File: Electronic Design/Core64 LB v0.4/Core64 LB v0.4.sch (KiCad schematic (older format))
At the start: 12 parts, among them J4 TSM-106-03-T-DV‎, U2 Teensy3.2, U3 M24C01-RMN, U4 SN74LV1T125DBVR

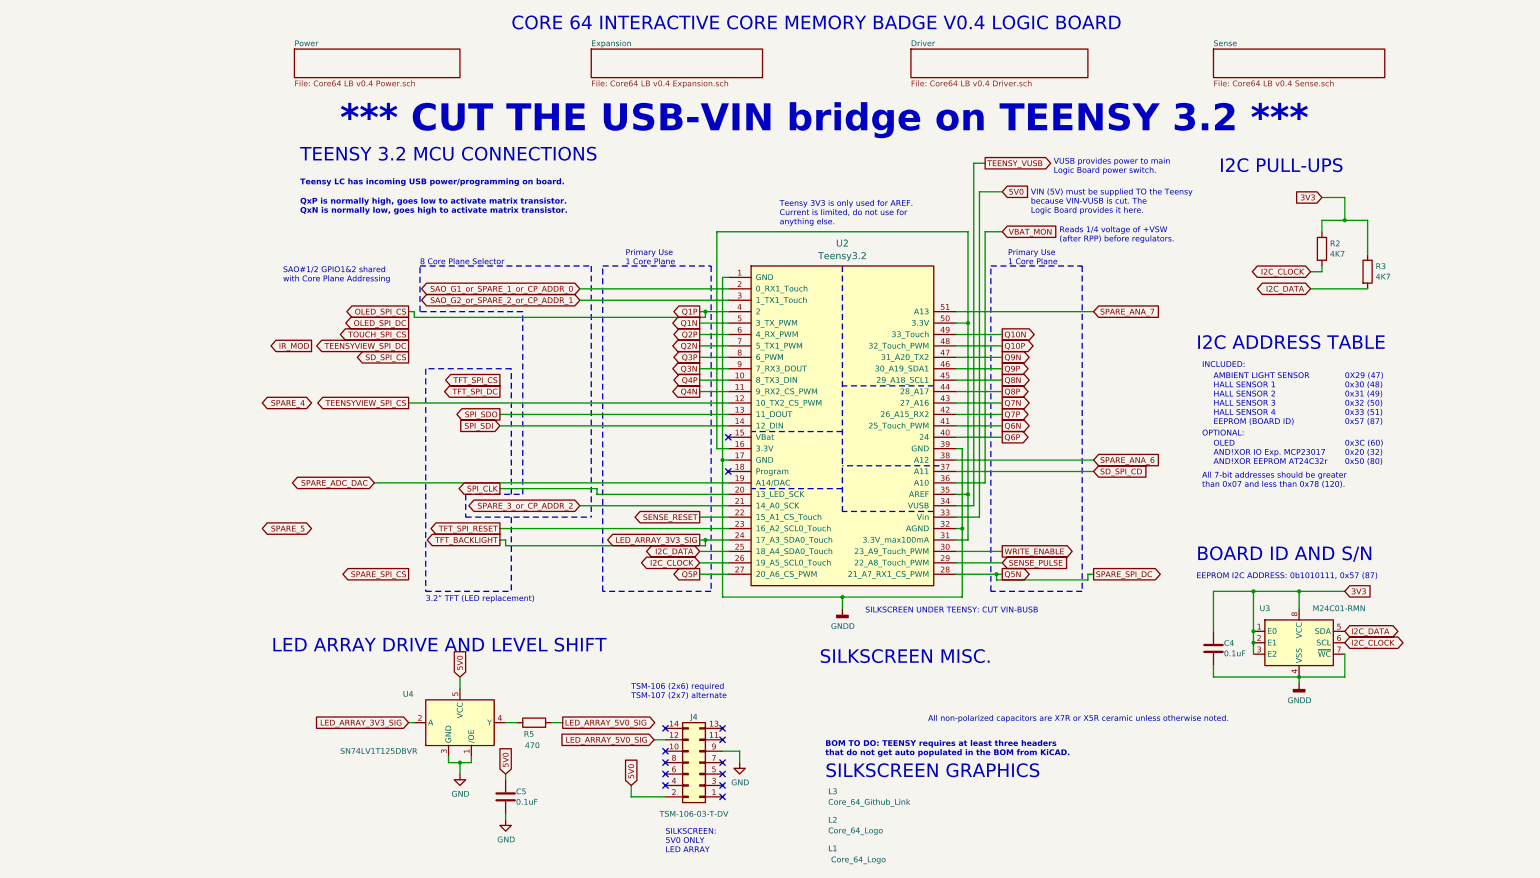
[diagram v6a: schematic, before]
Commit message: Refine LB Schem, RTC clock bat, PROG pin, LED array compact
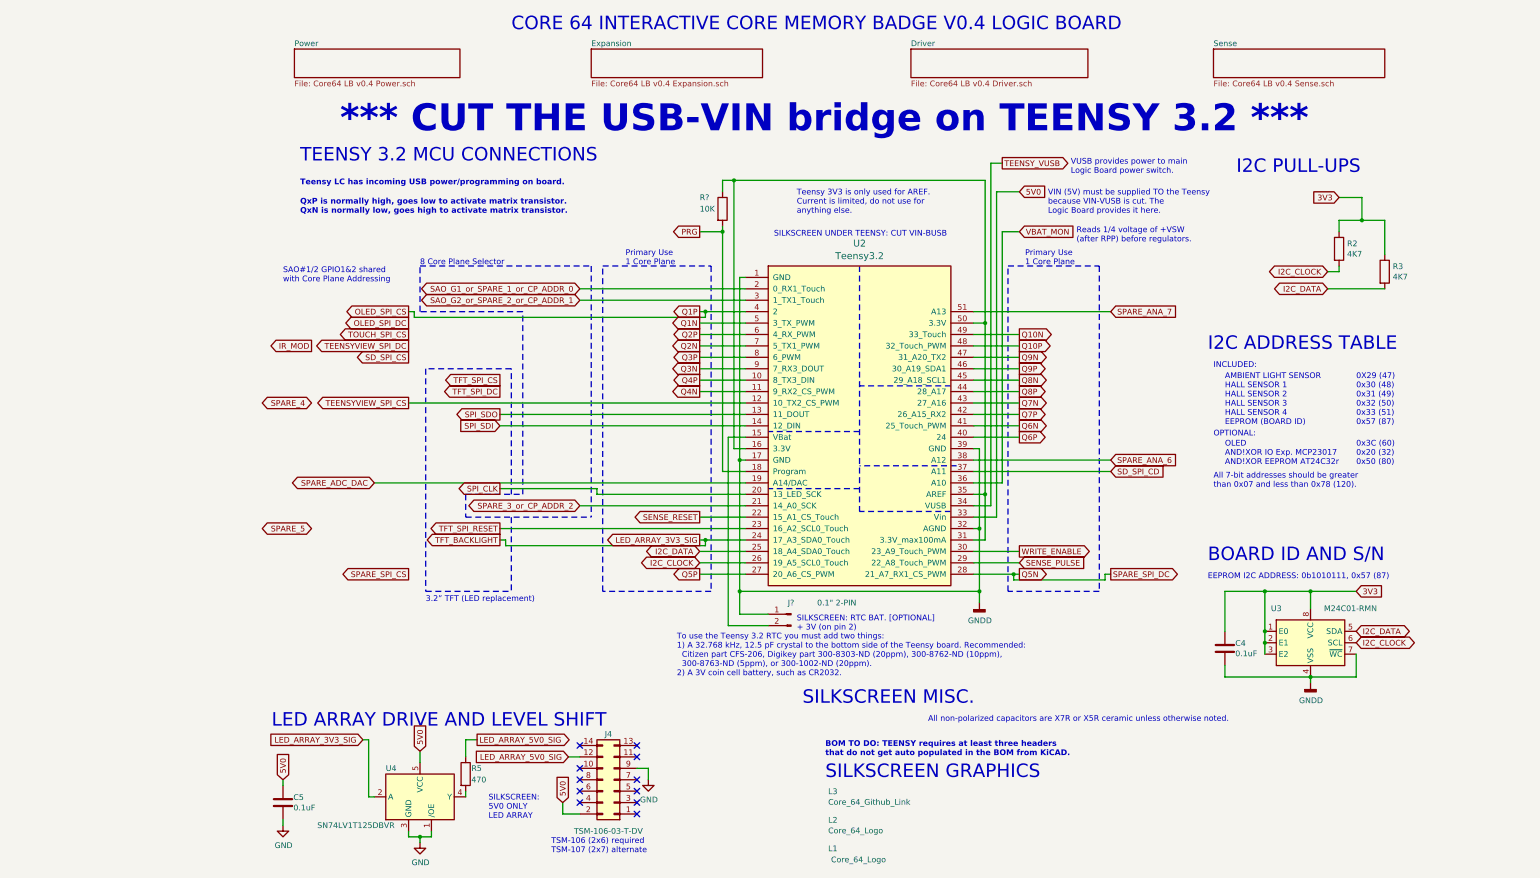
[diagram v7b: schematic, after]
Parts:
- added J?: 0.1\" 2-PIN, Connector_PinSocket_2.54mm:PinSocket_1x02_P2.54mm_Vertical_SMD_Pin1Left, symbol Connector:Conn_01x02_Male
- added R?: 10K, Resistor_SMD:R_0805_2012Metric, symbol Device:R
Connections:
- net GNDD: now also J?.1 (Pin_1)
- net LED_ARRAY_5V0_SIG: now also R5.1; no longer R5.2
- net at U4.4 (Y): now also R5.2; no longer R5.1
- net at U2.15 (VBat): now also J?.2 (Pin_2)
- net at U2.16 (3.3V), U2.31 (3.3V_max100mA), U2.35 (AREF)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: now also R?.1
- net PRG: now reaches U2.18 (Program)
- net PRG: now also R?.2
- no-connect marks 13 -> 11
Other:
- note added: "SILKSCREEN: RTC BAT. [OPTIONAL]\n+ 3V (on pin 2)"
- note added: "To use the Teensy 3.2 RTC you must add two things:\n1) A 32.768 kHz, 12.5 pF crystal to the bottom side of the Teensy board. Recommended: \n Citizen part CFS-206, Digikey part 300-8303-ND (20ppm), 300-8762-ND (10ppm), \n 300-8763-ND (5ppm), or 300-1002-ND (20ppm).\n2) A 3V coin cell battery, such as CR2032."
- moved on the sheet: C4, C5, J4, R2, R3, R5, U2, U3, U4

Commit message: Update schematic
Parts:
- removed C4, C5: 0.1uF, Capacitor_SMD:C_0805_2012Metric, symbol Device:C
- removed J4: TSM-106-03-T-DV‎, Connector_PinHeader_2.54mm:PinHeader_2x07_P2.54mm_Vertical_SMD_and_TH, symbol Connector_Generic:Conn_02x07_Odd_Even
- removed J?: 0.1\" 2-PIN, Connector_PinSocket_2.54mm:PinSocket_1x02_P2.54mm_Vertical_SMD_Pin1Left, symbol Connector:Conn_01x02_Male
- removed R5: 470, Resistor_SMD:R_0805_2012Metric, symbol Device:R
- removed U3: M24C01-RMN, Package_SO:SOIC-8_3.9x4.9mm_P1.27mm, symbol Memory_EEPROM:M24C01-RMN
- removed U4: SN74LV1T125DBVR, Package_TO_SOT_SMD:SOT-23-5, symbol Logic_LevelTranslator:SN74LV1T125DBVR
- added BT1: 3V, Battery:BatteryHolder_MPD_BC2003_1x2032, symbol Device:Battery_Cell
- added J12: TEENSY Cur. Mon., Connector_PinSocket_2.54mm:PinSocket_1x02_P2.54mm_Vertical, symbol Connector_Generic:Conn_01x02
- added J4: PRG, Connector_PinSocket_2.54mm:PinSocket_1x01_P2.54mm_Vertical, symbol Connector_Generic:Conn_01x01
- added R10, R44, R45, R46, R47, R48: 10K, Resistor_SMD:R_0805_2012Metric, symbol Device:R
- R2, R3: value 4K7 -> 2K2
- gave numbers to parts that had none: 1
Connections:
- net Q1N is gone; now on net OLED_SPI_DC: U2.5 (3_TX_PWM)
- net TEENSYVIEW_SPI_CS is gone; now on net SPARE_4: U2.12 (10_TX2_CS_PWM)
- net TFT_SPI_RESET is gone; now on net SENSE_RESET: U2.23 (16_A2_SCL0_Touch)
- net 3V3: now also R10.1, R44.1, R45.1, R46.1, R47.1, R48.1
- net 5V0: now also J12.1 (Pin_1), J12.2 (Pin_2)
- net GNDD: now also BT1.2 (-)
- net OLED_SPI_CS: now also R47.2
- net Q2P: now also R46.2
- net Q3P: now also R45.2
- net Q4P: now also R44.2
- net Q5P: now also R48.2
- net SENSE_RESET: no longer U2.22 (15_A1_CS_Touch)
- net SPARE_4: now also R10.2
- net SPARE_5: now also U2.22 (15_A1_CS_Touch)
- net at U2.15 (VBat): now also BT1.1 (+)
- net TEENSY_3V3: now reaches R5.1, U2.16 (3.3V), U2.31 (3.3V_max100mA), U2.35 (AREF), U2.50 (3.3V)
- net PRG: no longer names the net of R5.2, U2.18 (Program)
- net PRG: now also J4.1 (Pin_1)
- net Q2N renamed IR_MOD_OUT
- no-connect marks 11 -> 0
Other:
- note added: "1)"
- note added: "1) Serial Number Sticker Zone\n2) Board name, version, date, Machine Ideas"
- note added: "SILKSCREEN BACK"
- note added: "SILKSCREEN FRONT"
- note added: "SILKSCREEN: RTC BAT. CR2032\n[OPTIONAL]"
- note added: "SPI CS PULL-UPS"
- note added: "To use the Teensy 3.2 RTC you must add two things:\n1) Crystal: 32.768 kHz, 12.5 pF Citizen CFS-206, Digi-Key 300-8763-ND (5ppm)\n (on bottom side of the Teensy board)\n2) Battery Holder: MPD BC-2003, Digi-Key BC-2003-TR-CT-ND\n3) Battery: 3V CR2032 Digi-Key P189-ND\n (battery and holder on backside of logic board)\n"
- note removed: "0X29 (47)\n0x30 (48)\n0x31 (49)\n0x32 (50)\n0x33 (51)\n0x57 (87)"
- note removed: "0x3C (60)\n0x20 (32)\n0x50 (80)"
- note removed: "AMBIENT LIGHT SENSOR\nHALL SENSOR 1\nHALL SENSOR 2\nHALL SENSOR 3\nHALL SENSOR 4\nEEPROM (BOARD ID)"
- note removed: "All 7-bit addresses should be greater\nthan 0x07 and less than 0x78 (120)."
- note removed: "BOARD ID AND S/N"
- note removed: "EEPROM I2C ADDRESS: 0b1010111, 0x57 (87)"
- note removed: "I2C ADDRESS TABLE"
- note removed: "INCLUDED:"
- note removed: "LED ARRAY DRIVE AND LEVEL SHIFT"
- note removed: "OLED\nAND!XOR IO Exp. MCP23017\nAND!XOR EEPROM AT24C32r"
- note removed: "OPTIONAL:"
- note removed: "SILKSCREEN MISC."
- note removed: "SILKSCREEN: RTC BAT. [OPTIONAL]\n+ 3V (on pin 2)"
- note removed: "SILKSCREEN: \n5V0 ONLY\nLED ARRAY"
- note removed: "TSM-106 (2x6) required\nTSM-107 (2x7) alternate"
- note removed: "To use the Teensy 3.2 RTC you must add two things:\n1) A 32.768 kHz, 12.5 pF crystal to the bottom side of the Teensy board. Recommended: \n Citizen part CFS-206, Digikey part 300-8303-ND (20ppm), 300-8762-ND (10ppm), \n 300-8763-ND (5ppm), or 300-1002-ND (20ppm).\n2) A 3V coin cell battery, such as CR2032."
- moved on the sheet: R2, R3
